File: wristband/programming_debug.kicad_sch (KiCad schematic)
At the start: 1 part, among them J3 Conn_ARM_JTAG_SWD_10

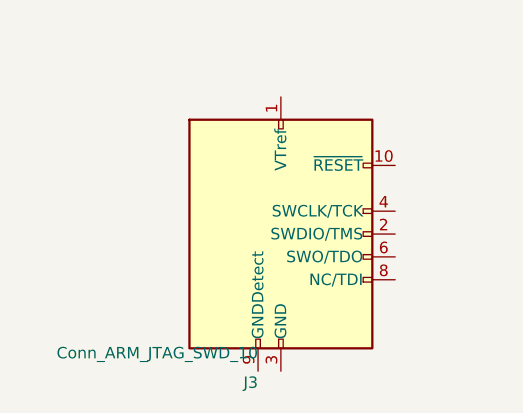
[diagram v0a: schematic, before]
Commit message: Migrate wristband to NINA-B400, wire all sheets, close six design gaps
Replaces the wristband's u-blox NINA-B111 (nRF52832) with a NINA-B400-00B
(Nordic nRF52833, Bluetooth 5.1), then follows through on everything that
change and a full schematic review surfaced.

NINA-B400 migration
- New 55-pin + EGP + EAGP symbol, transcribed from the real NINA-B40 data
  sheet UBX-19049405 R09 Table 6 and cross-checked against Figure 3 for rank
  ordering. Pin numbering validated programmatically (1-55, each exactly once).
- NINA-B4 is pin/mechanically compatible with NINA-B3, NOT NINA-B1, so the
  42-pad NINA111-42 land pattern does not carry over. No official footprint
  exists anywhere -- u-blox's own Eagle library ships only NINA111-42/112-42,
  and neither KiCad's bundled nor upstream RF_Module library has a B3/B4 part.
  NINA-B400-55_PLACEHOLDER is therefore flagged: outline, pad count and rank
  arrangement are confirmed; individual pad X/Y are derived estimates.
  MUST be replaced before fabrication.
- B400 chosen over B401/B406 for its on-module U.FL connector, which let the
  PCB-side U.FL (J2) and the untuned L/C match network (L1/C13) be deleted --
  retiring the project's only open RF-tuning risk.
- No power-design impact: abs-max VCC is 3.9 V on both modules, so the MCP1700
  LDO rationale stands. Budget 12 mA -> 15.5 mA typ; ~70.5 mA with DWM3000
  against 250 mA, ~3.5x headroom (corrects a stale "3.7x" in the docs).
- SWD pin numbers are unchanged (SWDCLK=11, SWDIO=15, RESET_N=19, SWO=8).

Antenna re-verified, part number corrected
- The specified antenna is still pre-approved for NINA-B4 (certification app
  note UBX-20037320 R05 s3.2) but ProAnt was acquired by Abracon and u-blox
  now lists it as PRO-IS-237. Same specs throughout. Order under the Abracon PN.

Six gaps closed
- Y1 + C14/C15: 32.768 kHz LFXO (Epson FC-135, Q13FC13500004). Required for
  lowest sleep current per SIM UBX-19052230 R13 s1.9; XL1/XL2 were floating,
  which Table 6 does not permit eve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
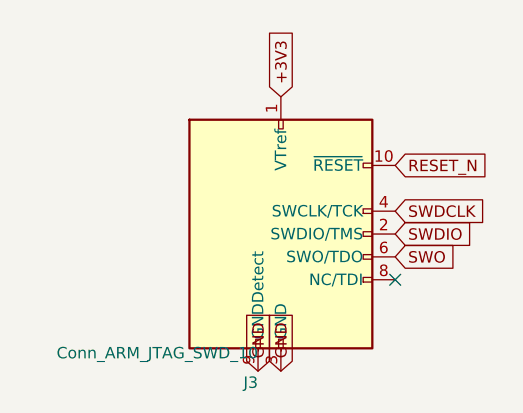
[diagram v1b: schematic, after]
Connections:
- net +3V3: now reaches J3.1 (VTref)
- net RESET_N: now reaches J3.10 (~{RESET})
- net SWDIO: now reaches J3.2 (SWDIO/TMS)
- net GND: now reaches J3.3 (GND), J3.5 (GND)
- net GND: now also J3.9 (GNDDetect)
- net SWDCLK: now reaches J3.4 (SWCLK/TCK)
- net SWO: now reaches J3.6 (SWO/TDO)
- no-connect marks 0 -> 1
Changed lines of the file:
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@@
 	(title_block
 		(title "Programming / Debug")
-		(comment 1 "Wristband NINA-B111 SWD/debug header -- placement only, not yet wired")
+		(comment 1 "Wristband NINA-B400 SWD/debug header -- placement only, not yet wired")
 	)
 	(symbol
@@
 		)
 	)
+	(global_label "+3V3"
+		(shape input)
+		(at 101.6 60.96 90)
+		(effects
+			(font
+				(size 1.27 1.27)
+			)
+			(justify left)
+		)
+	)
+	(global_label "SWDIO"
+		(shape input)
+		(at 114.3 76.2 0)
+		(effects
+			(font
+				(size 1.27 1.27)
+			)
+			(justify left)
+		)
+	)
+	(global_label "GND"
+		(shape input)
+		(at 101.6 91.44 270)
+		(effects
+			(font
+				(size 1.27 1.27)
+			)
+			(justify left)
+		)
+	)
+	(global_label "SWDCLK"
+		(shape input)
+		(at 114.3 73.66 0)
+		(effects
+			(font
+				(size 1.27 1.27)
+			)
+			(justify left)
+		)
+	)
+	(global_label "SWO"
+		(shape input)
+		(at 114.3 78.74 0)
+		(effects
+			(font
+				(size 1.27 1.27)
+			)
+			(justify left)
+		)
+	)
+	(global_label "GND"
+		(shape input)
+		(at 99.06 91.44 270)
+		(effects
+			(font
+				(size 1.27 1.27)
+			)
+			(justify left)
+		)
+	)
+	(global_label "RESET_N"
+		(shape input)
+		(at 114.3 68.58 0)
+		(effects
+			(font
+				(size 1.27 1.27)
+			)
+			(justify left)
+		)
+	)
+	(no_connect
+		(at 114.3 81.28)
+	)
 )

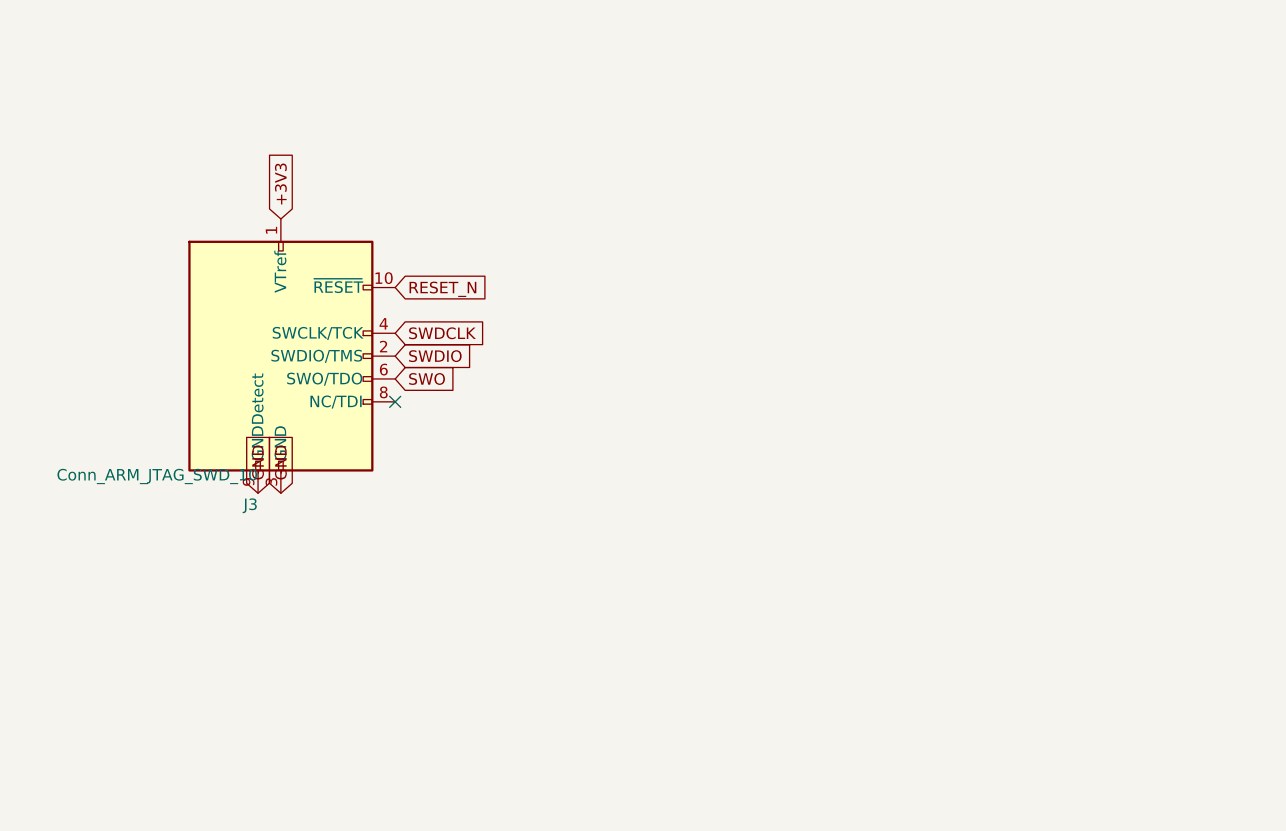
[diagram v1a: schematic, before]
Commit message: Make schematics readable: wire stubs, A3 reflow, DWM3000 symbol redraw
Connectivity is unchanged -- verified by diffing the exported netlist against
the previous commit: 34 nets, identical pin membership on every one. This is
presentation only.

The problem was pre-existing, not new. Labels were placed exactly on the pin
endpoint, so label text printed on top of the symbol's own pin name (+3V3
stamped over VCC, UWB_CS over GPIO_1). power_bms had it on U1/U2/Q2 as well;
it only became obvious when the convention was scaled onto a 55-pin part.
Every label now sits at the end of a short wire stub pointing away from the
body, which is the standard KiCad idiom.

DWM3000 symbol redrawn (shared/symbols/)
- The old symbol was a 20mm square carrying pin names like GPIO0/RXOKLED drawn
  vertically along the bottom edge, where they collided with each other inside
  the symbol. No amount of label placement fixes that.
- Now 56 x 41mm, functionally grouped: power/ground/control left, SPI/GPIO
  right, no bottom-edge pins. All 24 pins and every property preserved.
- Checked the blast radius before touching it: bay-station is entirely unwired
  (0 wires, 0 labels on every sheet), so nothing was orphaned. Its cached copy
  is refreshed here and its netlist still exports cleanly at 75 components.

Layout
- radio_mcu and power_bms moved to A3 and reflowed into functional blocks;
  42 symbols repositioned.
- 38 annotations added, carrying the datasheet citations and reasoning that
  previously lived only in the markdown -- LFXO load-cap derivation, the
  ~2.1uA battery-divider tradeoff, why DW01A's GND sits on CELL_N, the LDO
  headroom budget, and the unchanged-from-NINA-B111 SWD pin numbers.

Verification
- Wrote a text-collision checker rather than eyeballing it. It caught two
  classes of bug: duplicated annotations (strip() cleared labels and wires but
  not text, so a second pass layered notes over old ones) and doubled labels on
  stacked same-net pins (USB-C J1 A9/B9, A12/B12;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
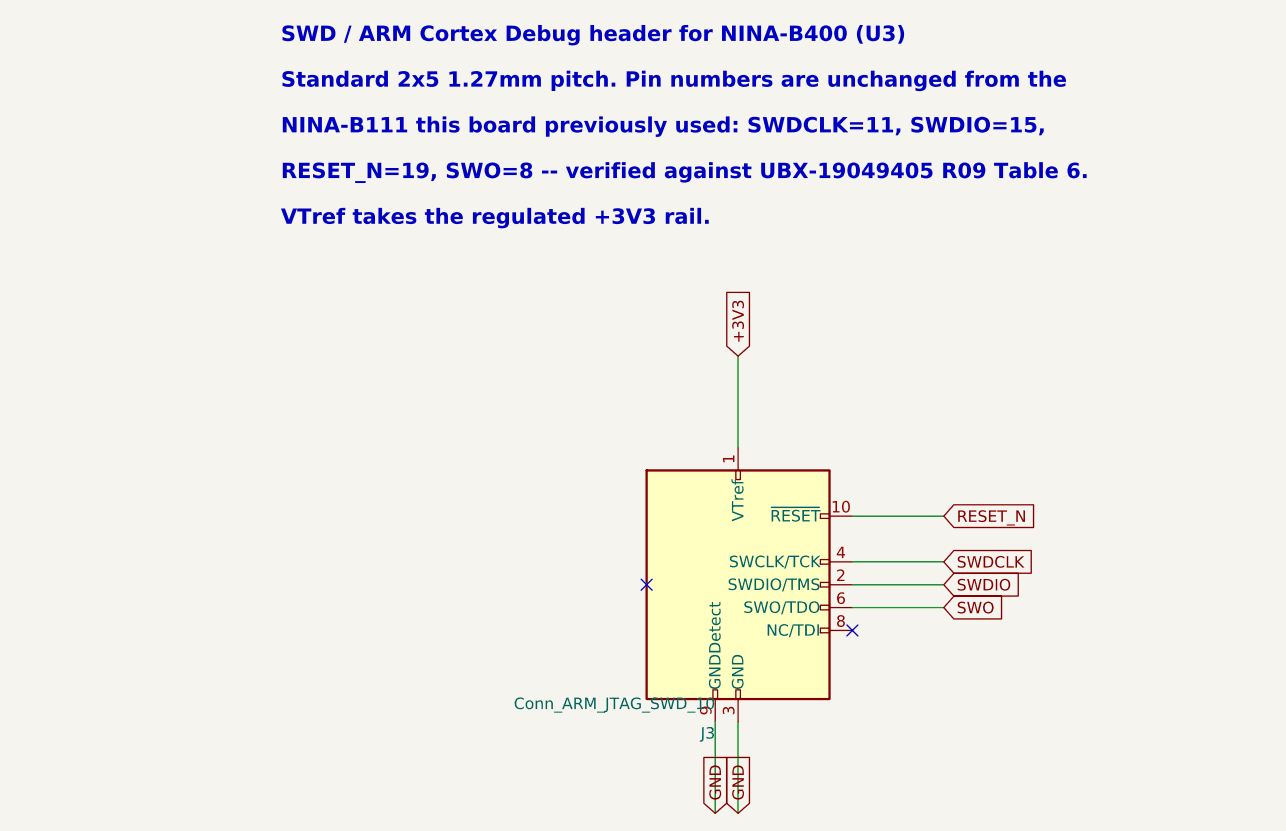
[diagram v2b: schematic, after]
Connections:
- no-connect marks 1 -> 2
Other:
- note added: "NINA-B111 this board previously used: SWDCLK=11, SWDIO=15,"
- note added: "RESET_N=19, SWO=8 -- verified against UBX-19049405 R09 Table 6."
- note added: "SWD / ARM Cortex Debug header for NINA-B400 (U3)"
- note added: "Standard 2x5 1.27mm pitch. Pin numbers are unchanged from the"
- note added: "VTref takes the regulated +3V3 rail."
- moved on the sheet: J3
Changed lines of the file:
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@@
 	(symbol
 		(lib_id "Connector:Conn_ARM_JTAG_SWD_10")
-		(at 101.6 76.2 0)
+		(at 152.4 101.6 0)
 		(unit 1)
 		(exclude_from_sim no)
@@
 		(dnp no)
 		(property "Reference" "J3"
-			(at 99.06 92.71 0)
+			(at 149.86 118.11 0)
 			(effects
 				(font
@@
 		)
 		(property "Value" "Conn_ARM_JTAG_SWD_10"
-			(at 99.06 90.17 0)
+			(at 149.86 115.57 0)
 			(effects
 				(font
@@
 		)
 		(property "Footprint" "Connector_PinHeader_1.27mm:PinHeader_2x05_P1.27mm_Vertical"
-			(at 101.6 76.2 0)
+			(at 152.4 101.6 0)
 			(effects
 				(font
@@
 		)
 		(property "Datasheet" ""
-			(at 101.6 76.2 0)
+			(at 152.4 101.6 0)
 			(effects
 				(font
@@
 		)
 	)
+	(wire
+		(pts
+			(xy 152.4 86.36) (xy 152.4 76.2)
+		)
+		(stroke
+			(width 0)
+			(type default)
+		)
+	)
 	(global_label "+3V3"
 		(shape input)
-		(at 101.6 60.96 90)
-		(effects
-			(font
-				(size 1.27 1.27)
-			)
-			(justify left)
+		(at 152.4 76.2 90)
+		(effects
+			(font
+				(size 1.27 1.27)
+			)
+			(justify left)
+		)
+	)
+	(wire
+		(pts
+			(xy 165.1 101.6) (xy 175.26 101.6)
+		)
+		(stroke
+			(width 0)
+			(type default)
 		)
 	)
 	(global_label "SWDIO"
 		(shape input)
-		(at 114.3 76.2 0)
-		(effects
-			(font
-				(size 1.27 1.27)
-			)
-			(justify left)
+		(at 175.26 101.6 0)
+		(effects
+			(font
+				(size 1.27 1.27)
+			)
+			(justify left)
+		)
+	)
+	(wire
+		(pts
+			(xy 152.4 116.84) (xy 152.4 127)
+		)
+		(stroke
+			(width 0)
+			(type default)
 		)
 	)
 	(global_label "GND"
 		(shape input)
-		(at 101.6 91.44 270)
-		(effects
-			(font
-				(size 1.27 1.27)
-			)
-			(justify left)
+		(at 152.4 127 270)
+		(effects
+			(font
+				(size 1.27 1.27)
+			)
+			(justify left)
+		)
+	)
+	(wire
+		(pts
+			(xy 165.1 99.06) (xy 175.26 99.06)
+		)
+		(stroke
+			(width 0)
+			(type default)
 		)
 	)
 	(global_label "SWDCLK"
 		(shape input)
-		(at 114.3 73.66 0)
-		(effects
-			(font
-				(size 1.27 1.27)
-			)
-			(justify left)
+		(at 175.26 99.06 0)
+		(effects
+			(font
+				(size 1.27 1.27)
+			)
+			(justify left)
+		)
+	)
+	(wire
+		(pts
+			(xy 165.1 104.14) (xy 175.26 104.14)
+		)
+		(stroke
+			(width 0)
+			(type default)
 		)
 	)
 	(global_label "SWO"
 		(shape input)
-		(at 114.3 78.74 0)
-		(effects
-			(font
-				(size 1.27 1.27)
-			)
-			(justify left)
+		(at 175.26 104.14 0)
+		(effects
+			(font
+				(size 1.27 1.27)
+			)
+			(justify left)
+		)
+	)
+	(wire
+		(pts
+			(xy 149.86 116.84) (xy 149.86 127)
+		)
+		(stroke
+			(width 0)
+			(type default)
 		)
 	)
 	(global_label "GND"
 		(shape input)
-		(at 99.06 91.44 270)
-		(effects
-			(font
-				(size 1.27 1.27)
-			)
-			(justify left)
+		(at 149.86 127 270)
+		(effects
+			(font
+				(size 1.27 1.27)
+			)
+			(justify left)
+		)
+	)
+	(wire
+		(pts
+			(xy 165.1 93.98) (xy 175.26 93.98)
+		)
+		(stroke
+			(width 0)
+			(type default)
 		)
 	)
 	(global_label "RESET_N"
 		(shape input)
-		(at 114.3 68.58 0)
-		(effects
-			(font
-				(size 1.27 1.27)
+		(at 175.26 93.98 0)
+		(effects
+			(font
+				(size 1.27 1.27)
+			)
+			(justify left)
+		)
+	)
+	(text "SWD / ARM Cortex Debug header for NINA-B400 (U3)"
+		(at 101.6 40.64 0)
+		(effects
+			(font
+				(size 1.7 1.7)
+				(bold yes)
+			)
+			(justify left)
+		)
+	)
+	(text "Standard 2x5 1.27mm pitch. Pin numbers are unchanged from the"
+		(at 101.6 45.72 0)
+		(effects
+			(font
+				(size 1.7 1.7)
+				(bold yes)
+			)
+			(justify left)
+		)
+	)
+	(text "NINA-B111 this board previously used: SWDCLK=11, SWDIO=15,"
+		(at 101.6 50.8 0)
+		(effects
+			(font
+				(size 1.7 1.7)
+				(bold yes)
+			)
+			(justify left)
+		)
+	)
+	(text "RESET_N=19, SWO=8 -- verified against UBX-19049405 R09 Table 6."
+		(at 101.6 55.88 0)
+		(effects
+			(font
+				(size 1.7 1.7)
+				(bold yes)
+			)
+			(justify left)
+		)
+	)
+	(text "VTref takes the regulated +3V3 rail."
+		(at 101.6 60.96 0)
+		(effects
+			(font
+				(size 1.7 1.7)
+				(bold yes)
 			)
 			(justify left)
@@
 	)
 	(no_connect
-		(at 114.3 81.28)
+		(at 142.24 101.6)
+	)
+	(no_connect
+		(at 165.1 106.68)
 	)
 )
